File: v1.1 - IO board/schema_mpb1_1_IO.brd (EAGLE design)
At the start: 178.4 x 47.8 mm, 94 parts

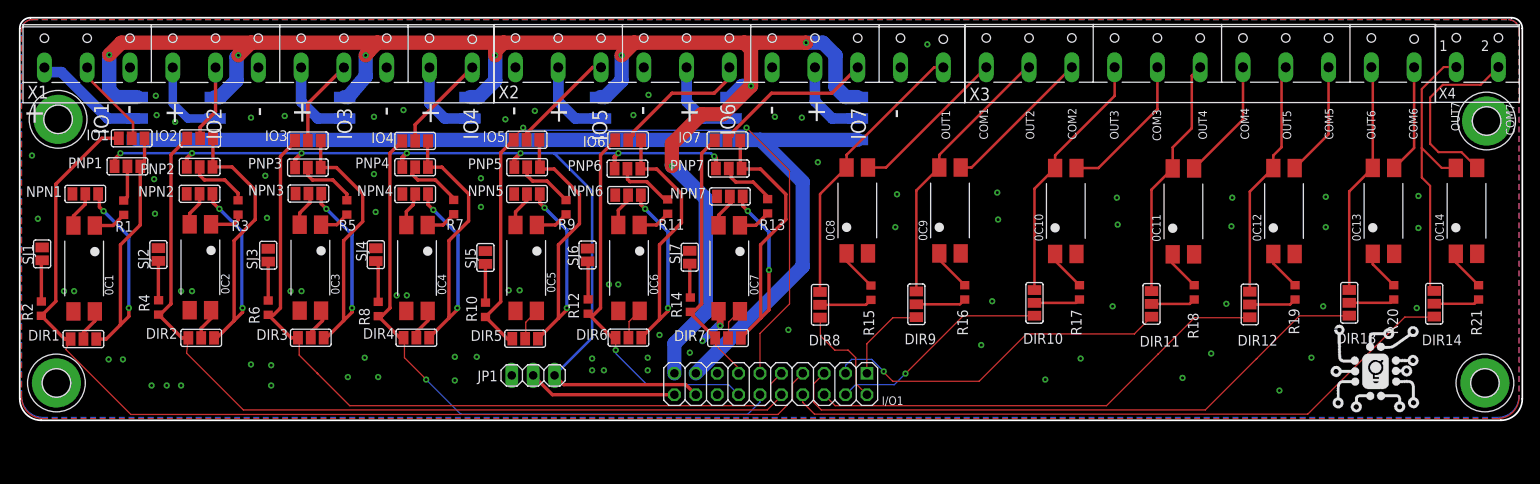
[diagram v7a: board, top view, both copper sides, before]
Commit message: IO board revision
- Made Output traces thicker
- Added pad for 5V/3.3V power for input sensors
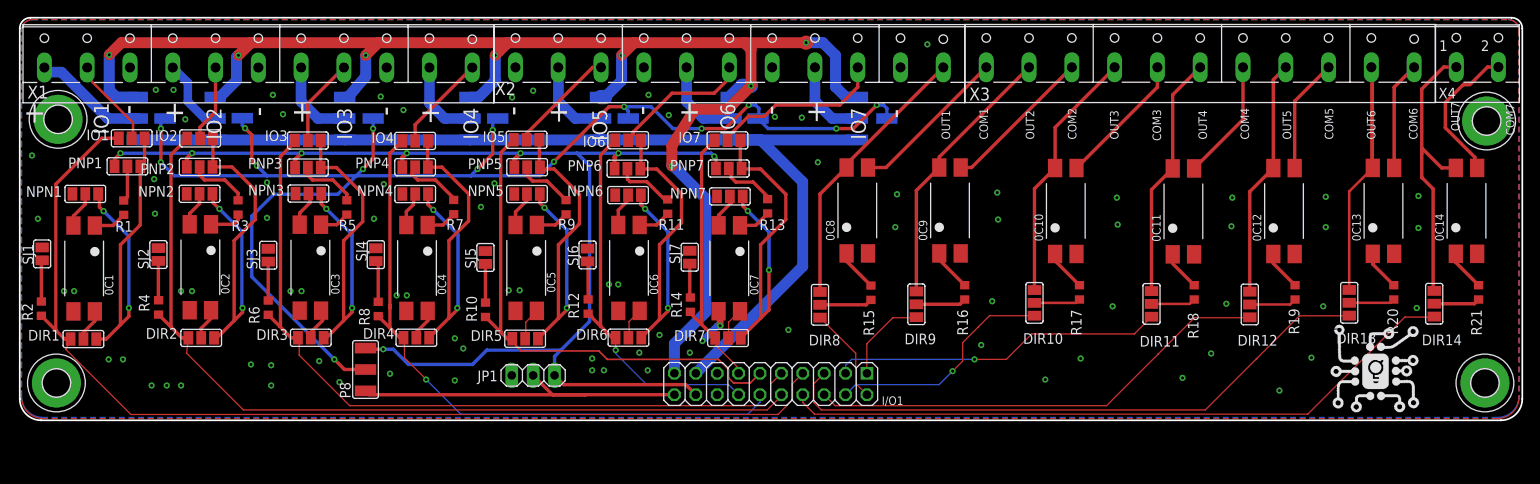
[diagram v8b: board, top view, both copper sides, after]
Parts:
- added P8: (no value), jumper:SJ_2W
- added PAD1, PAD2, PAD3, PAD4, PAD5, PAD6, PAD7: (no value), wirepad:SMD1,27-2,54
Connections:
- new net P8: P8.2, PAD1.1, PAD2.1, PAD3.1, PAD4.1, PAD5.1, PAD6.1, PAD7.1
- net +3V3: now also P8.3
- net +5V: now also P8.1
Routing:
- net P8: track 0.00 -> 168.6 mm, vias 0 -> 15
- net PE11: track 88.1 -> 60.6 mm, vias 2 -> 0
- net +5V: track 17.7 -> 44.0 mm
- net +3V3: track 131.6 -> 154.9 mm, vias 7 -> 8
- net OUT6: track 27.7 -> 39.8 mm
- net OUT7: track 34.8 -> 42.5 mm
- net COM7: track 21.9 -> 17.4 mm
- net +12V: track 192.3 -> 188.2 mm
- net PE3: track 41.9 -> 39.7 mm
- net COM3: track 17.5 -> 15.9 mm
- net IO7: track 19.3 -> 20.6 mm
- net PE2: track 26.3 -> 27.6 mm
- net P2: track 10.0 -> 8.87 mm
- net PE13: track 31.5 -> 32.6 mm
- net PE7: track 125.9 -> 127.0 mm
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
